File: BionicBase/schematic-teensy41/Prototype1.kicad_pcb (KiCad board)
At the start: 2 copper layers, 114 x 102 mm, 15 parts, among them J1 Bionic_ZIF_Socket_48pin, M1 TXS0108E, M2 TXS0108E, M3 TXS0108E, M4 TXS0108E, M5 TXS0108E, SW1 Tact_SW

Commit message: Migrate to KiCad 6.0
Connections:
- net /~USR_LED~ renamed /~{USR_LED}
- net /~USR_SW~ renamed /~{USR_SW}
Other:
- net class Default removed

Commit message: [BionicBase] Fix Teensy 4.1 base board
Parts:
- M1, M2, M3, M4, M5: value TXS0108E -> TXB0108
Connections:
- B1 pad 16: Net-(B1-Pad16) -> unconnected-(B1-Pad16)
- B1 pad 17: Net-(B1-Pad17) -> unconnected-(B1-Pad17)
- J1 pad 10: /E0 -> unconnected-(J1-Pad10)
- J1 pad 19: /E2 -> unconnected-(J1-Pad19)
- J1 pad 30: /E3 -> unconnected-(J1-Pad30)
- J1 pad 39: /E1 -> unconnected-(J1-Pad39)
- M3 pad 11: Net-(M3-Pad11) -> GND

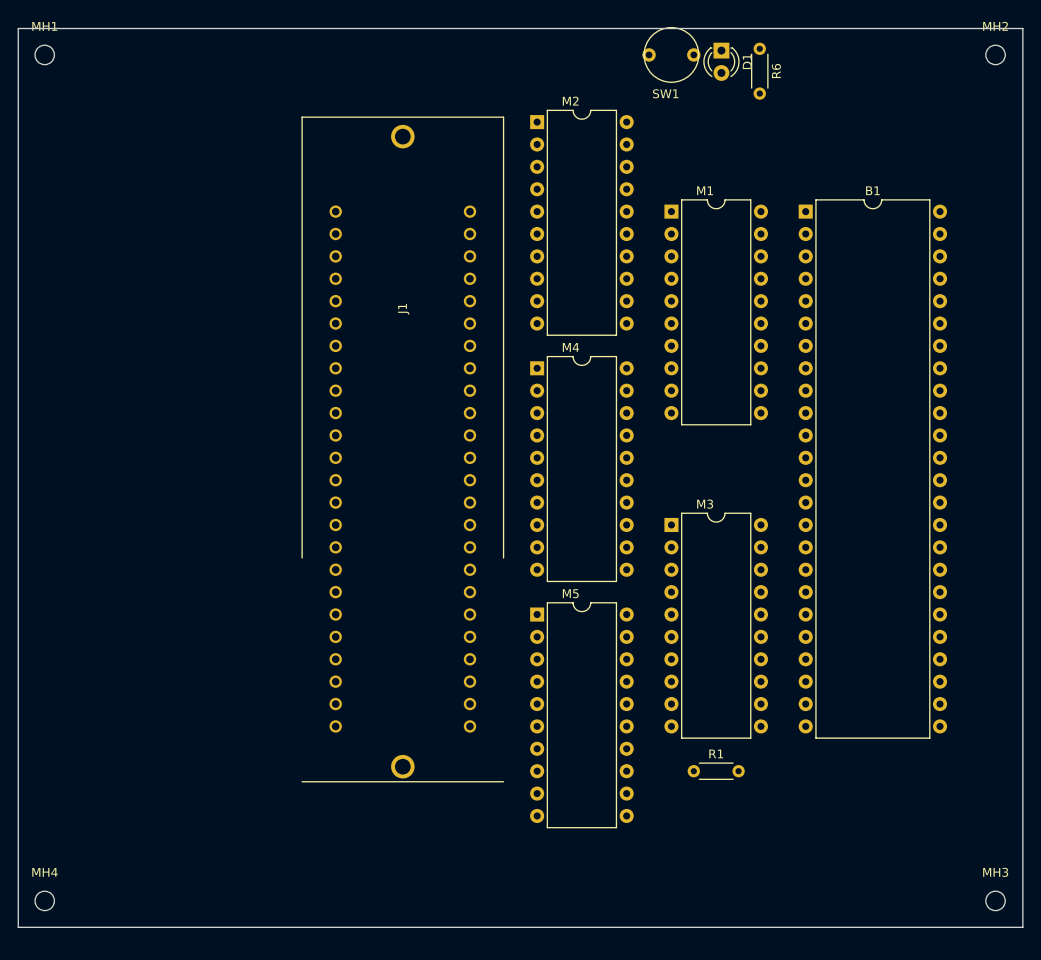
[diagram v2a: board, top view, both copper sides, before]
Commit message: [BionicBase] Add schematics using surface mount devices
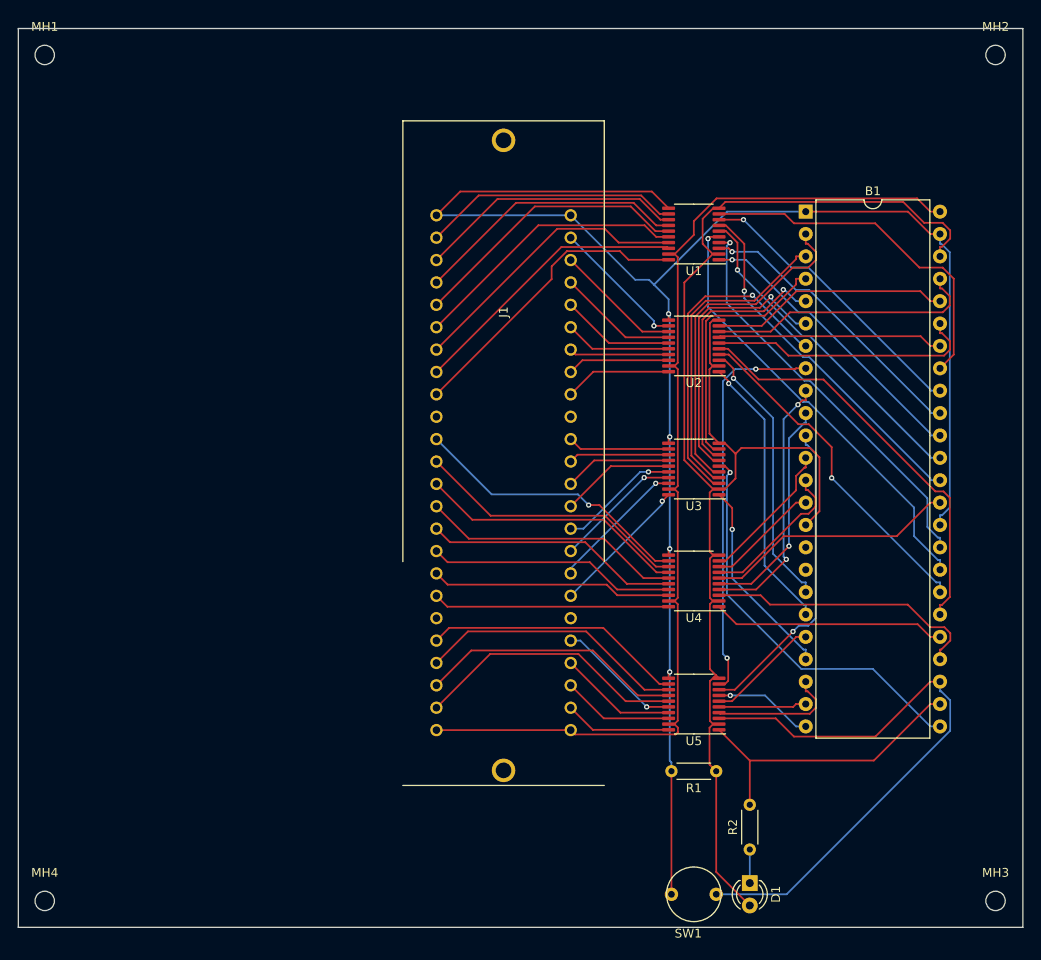
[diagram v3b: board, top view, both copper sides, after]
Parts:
- removed M1, M2, M3, M4, M5: TXB0108, 0-LocalLibrary:DIP-20_W10.16mm
- added U1: TXS0108EPW, Package_SO:TSSOP-20_4.4x6.5mm_P0.65mm, F.Cu at (149.3, 64.9)
- added U2: TXS0108EPW, Package_SO:TSSOP-20_4.4x6.5mm_P0.65mm, F.Cu at (149.3, 77.6)
- added U3: TXS0108EPW, Package_SO:TSSOP-20_4.4x6.5mm_P0.65mm, F.Cu at (149.3, 91.6)
- added U4: TXS0108EPW, Package_SO:TSSOP-20_4.4x6.5mm_P0.65mm, F.Cu at (149.3, 104.3)
- added U5: TXS0108EPW, Package_SO:TSSOP-20_4.4x6.5mm_P0.65mm, F.Cu at (149.3, 118.3)
- moved SW1 95.3 mm to (149.3, 139.8)
- moved D1 94.5 mm to (155.6, 138.6)
- moved R2 90.9 mm to (155.6, 134.8), turned to 90 degrees
- moved J1 11.4 mm to (127.7, 76.8)
- moved R1 2.54 mm to (151.8, 125.9), turned to 180 degrees
- renumbered R6 to R2
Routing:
- net GND: track 0.00 -> 200.3 mm, vias 0 -> 4
- net +3V3: track 0.00 -> 164.7 mm
- net VCC: track 0.00 -> 121.0 mm
- net /~{USR_SW}: track 0.00 -> 68.9 mm
- net Net-(B1-Pad32): track 0.00 -> 50.3 mm, vias 0 -> 1
- net Net-(B1-Pad30): track 0.00 -> 47.0 mm
- net Net-(B1-Pad33): track 0.00 -> 46.5 mm, vias 0 -> 1
- net Net-(B1-Pad25): track 0.00 -> 46.0 mm, vias 0 -> 1
- net Net-(B1-Pad8): track 0.00 -> 45.4 mm, vias 0 -> 2
- net Net-(B1-Pad36): track 0.00 -> 40.8 mm, vias 0 -> 1
- net Net-(B1-Pad41): track 0.00 -> 40.5 mm
- net Net-(B1-Pad2): track 0.00 -> 39.0 mm
- net Net-(B1-Pad31): track 0.00 -> 38.9 mm, vias 0 -> 1
- net Net-(B1-Pad7): track 0.00 -> 37.7 mm, vias 0 -> 1
- net Net-(B1-Pad37): track 0.00 -> 37.7 mm, vias 0 -> 1
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
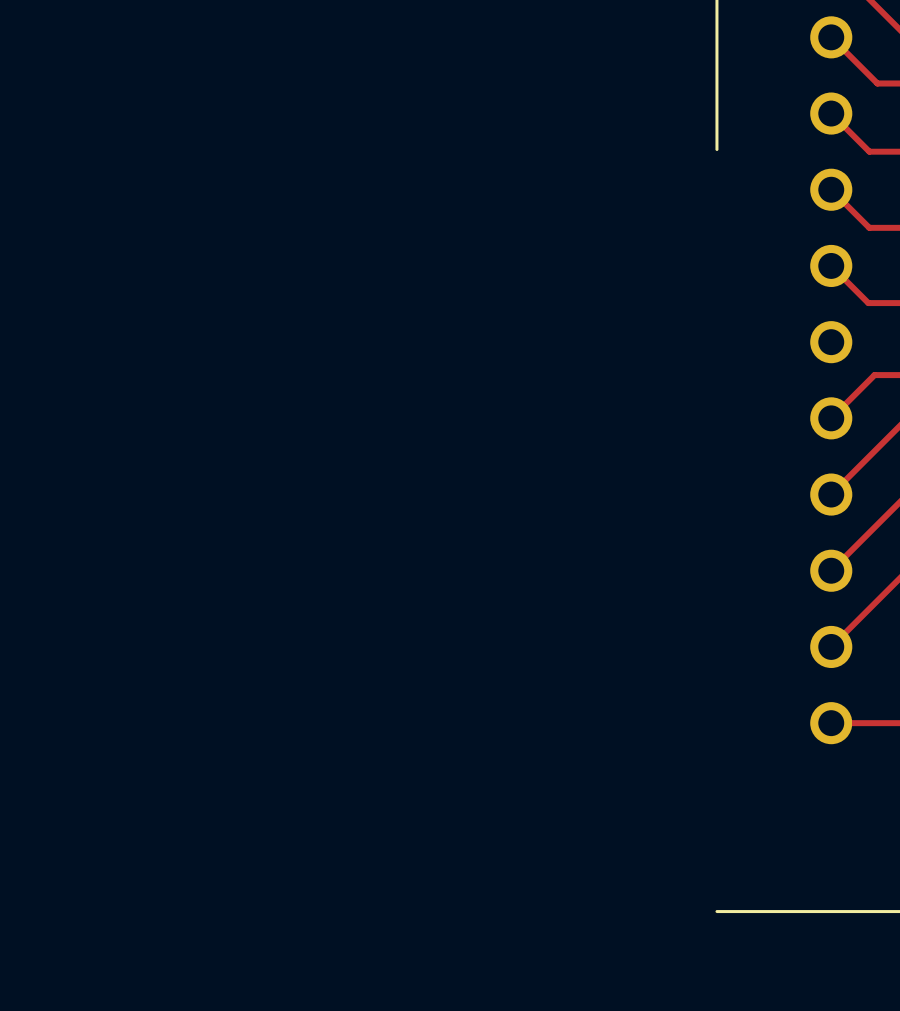
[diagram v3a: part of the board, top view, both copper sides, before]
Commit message: [BionicBase] Add DC-DC Converter for +15V
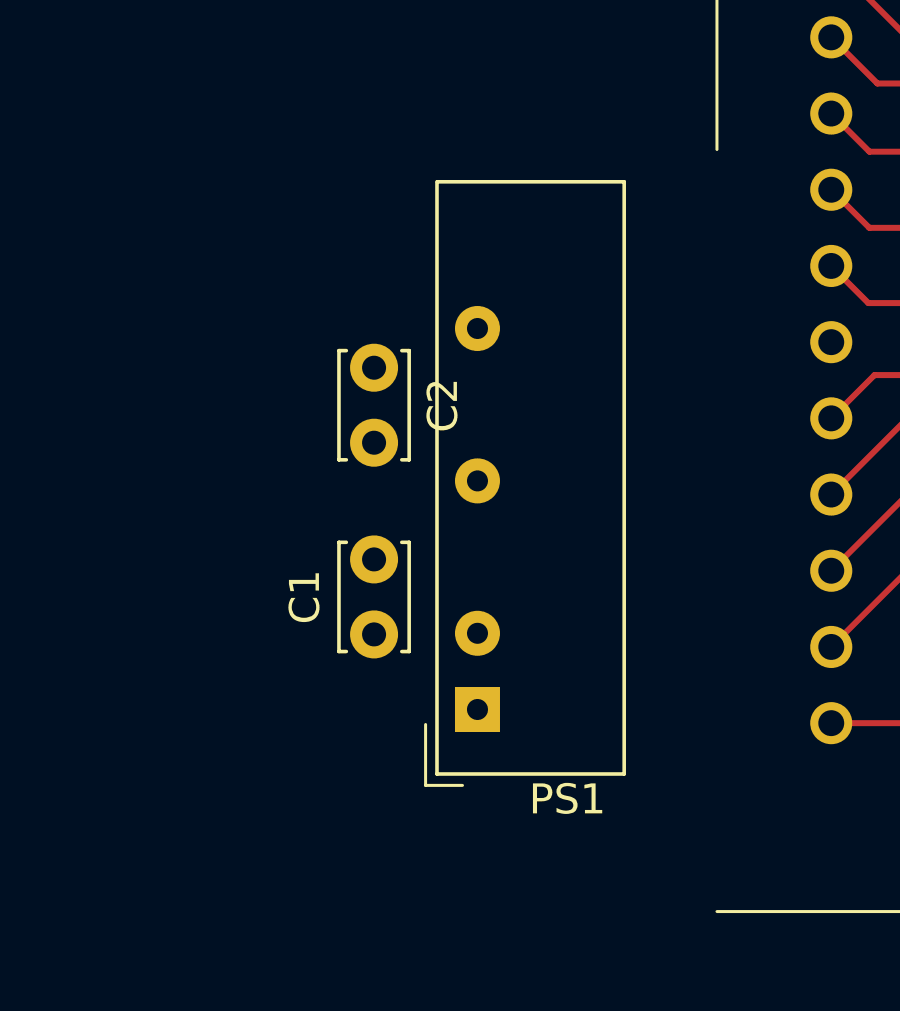
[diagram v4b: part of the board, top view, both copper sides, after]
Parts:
- added C1: 2.2u, Capacitor_THT:C_Disc_D3.4mm_W2.1mm_P2.50mm, F.Cu at (104.8, 118.3)
- added C2: 1.0u, Capacitor_THT:C_Disc_D3.4mm_W2.1mm_P2.50mm, F.Cu at (104.8, 109.4)
- added PS1: MAU105, 0-LocalLibrary:Converter_DCDC_Minmax_MAU100_THT, F.Cu at (108.3, 120.8)
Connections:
- net +3V3 renamed +3.3V
- J1 pad 19: unconnected-(J1-Pad19) -> /+15V
- J1 pad 30: unconnected-(J1-Pad30) -> /+15V

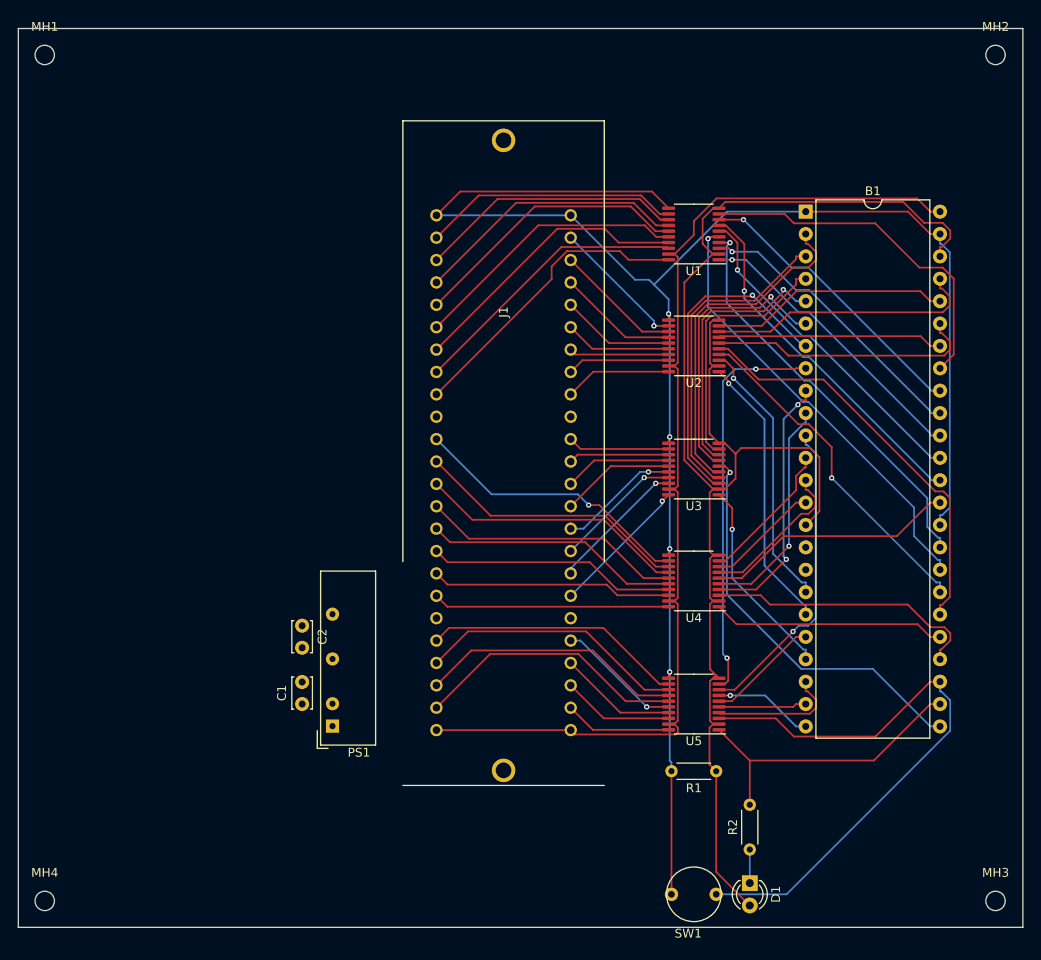
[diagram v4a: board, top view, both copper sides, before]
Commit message: [BionicBase] Add ID EEPROM and change SW and LED conections
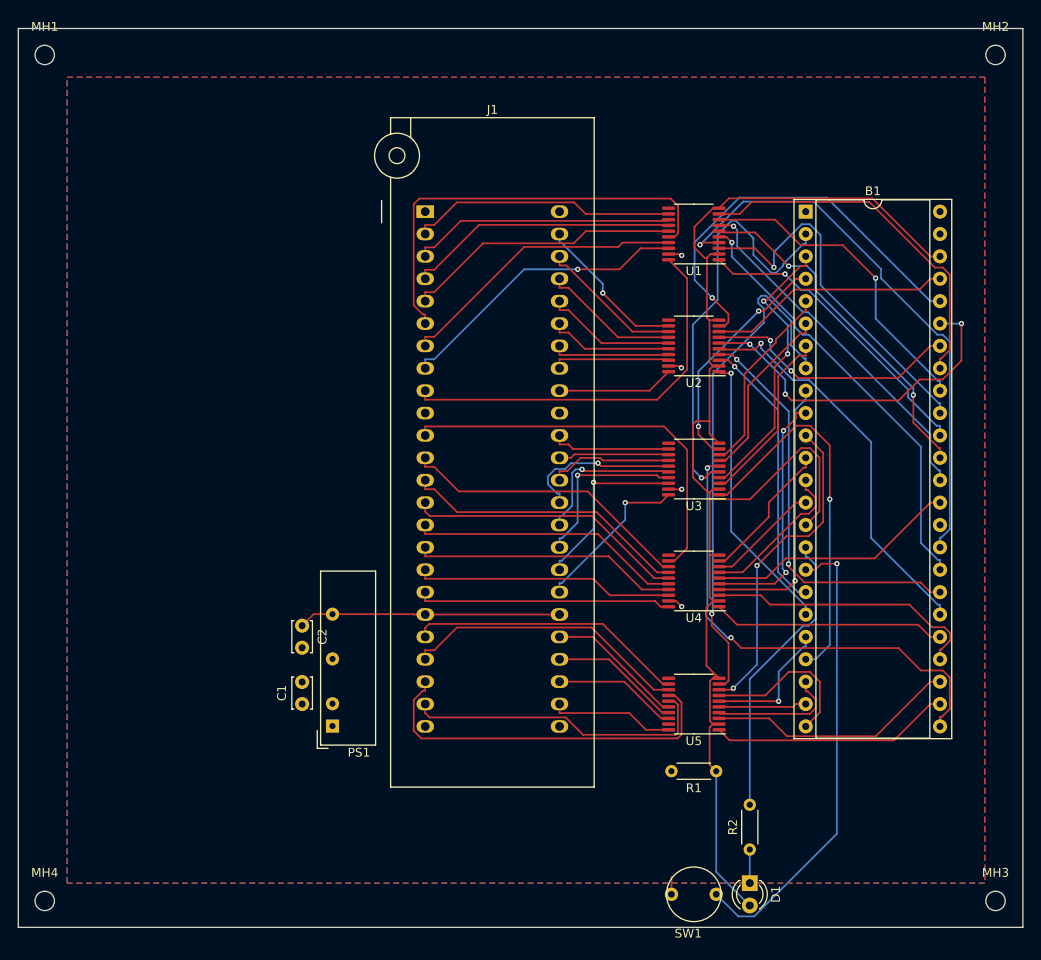
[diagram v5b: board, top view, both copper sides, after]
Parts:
- B1: footprint Package_DIP:DIP-48_W15.24mm -> Package_DIP:DIP-48_W15.24mm_Socket
- J1: footprint 0-LocalLibrary:Aries_ZIF_socket_DIP-48-pin -> 0-LocalLibrary:Aries-57-DIP48
- moved J1 16.9 mm to (118.8, 62.4)
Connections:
- B1 pad 16: unconnected-(B1-P6.12-Pad16) -> Net-(B1-P6.12)
- B1 pad 17: unconnected-(B1-P6.13-Pad17) -> Net-(B1-P6.13)
- R2 pad 2: /~{USR_LED} -> Net-(B1-P6.12)
- SW1 pad 1: /~{USR_SW} -> Net-(B1-P6.13)
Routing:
- net GND: track 200.3 -> 1.98 mm, vias 4 -> 0
- net VCC: track 121.0 -> 6.35 mm, vias 0 -> 4
- net Net-(B1-P6.13): track 0.00 -> 53.1 mm, vias 0 -> 1
- net /~{USR_SW}: track 68.9 -> 28.5 mm
- net Net-(B1-P6.12): track 0.00 -> 33.3 mm
- net /+15V: track 0.00 -> 29.8 mm
- net Net-(B1-P9.31): track 22.9 -> 42.8 mm
- net Net-(B1-P6.24): track 27.2 -> 46.7 mm, vias 0 -> 1
- net /P14: track 31.7 -> 49.2 mm
- net Net-(B1-P6.21): track 46.5 -> 63.7 mm
- net Net-(B1-P9.08): track 37.7 -> 20.5 mm, vias 1 -> 0
- net +3.3V: track 164.7 -> 150.1 mm
- net Net-(B1-P7.10): track 45.4 -> 59.3 mm, vias 2 -> 1
- net /P30: track 32.1 -> 45.7 mm, vias 1 -> 0
- net /P52: track 30.1 -> 42.6 mm
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- added copper zone on F.Cu, net GND
- added copper zone on B.Cu, net VCC
